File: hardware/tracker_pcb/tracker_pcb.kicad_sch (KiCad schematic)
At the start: 19 parts, among them J1 JL308-25412G01, J2 B6B-PH-K-S, J3 256-406, J5 B4B-XH-A, X1 256-402

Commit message: wip
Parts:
- JP1, JP10, JP2, JP3, JP4, JP9: now in the parts list
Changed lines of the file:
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@@
 		(unit 1)
 		(exclude_from_sim no)
-		(in_bom no)
+		(in_bom yes)
 		(on_board yes)
 		(dnp no)
@@
 		(unit 1)
 		(exclude_from_sim no)
-		(in_bom no)
+		(in_bom yes)
 		(on_board yes)
 		(dnp no)
@@
 		(unit 1)
 		(exclude_from_sim no)
-		(in_bom no)
+		(in_bom yes)
 		(on_board yes)
 		(dnp no)
@@
 		(unit 1)
 		(exclude_from_sim no)
-		(in_bom no)
+		(in_bom yes)
 		(on_board yes)
 		(dnp no)
@@
 		(unit 1)
 		(exclude_from_sim no)
-		(in_bom no)
+		(in_bom yes)
 		(on_board yes)
 		(dnp no)
@@
 		(unit 1)
 		(exclude_from_sim no)
-		(in_bom no)
-		(on_board yes)
-		(dnp no)
+		(in_bom yes)
+		(on_board yes)
+		(dnp no)

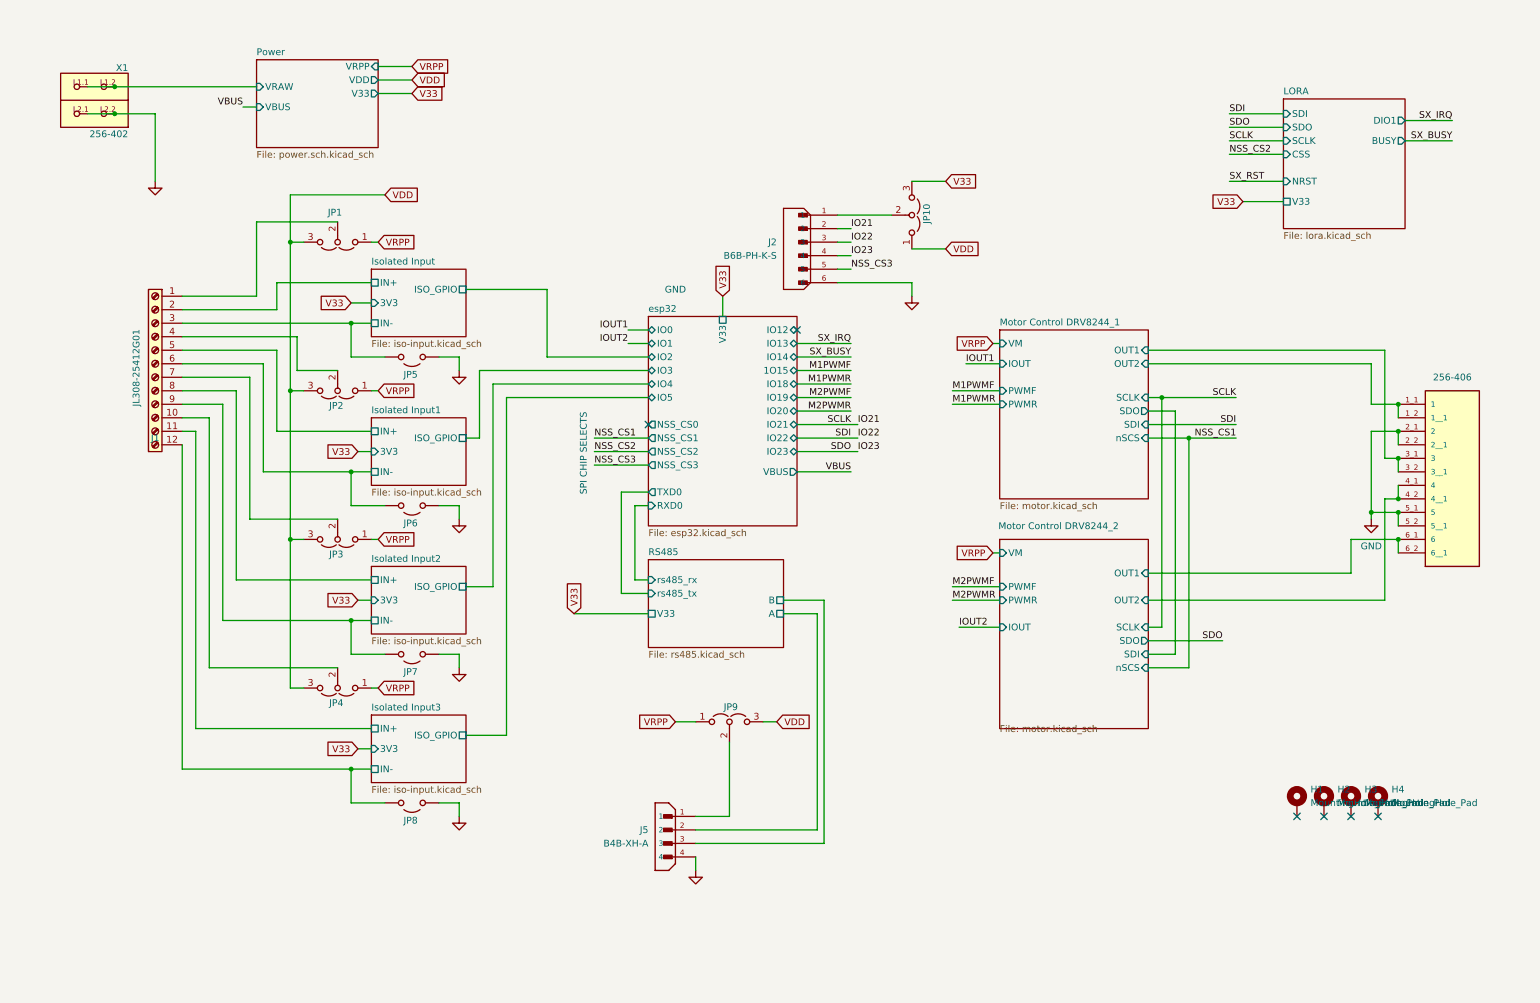
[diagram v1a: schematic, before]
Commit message: Add jst xh for inputs
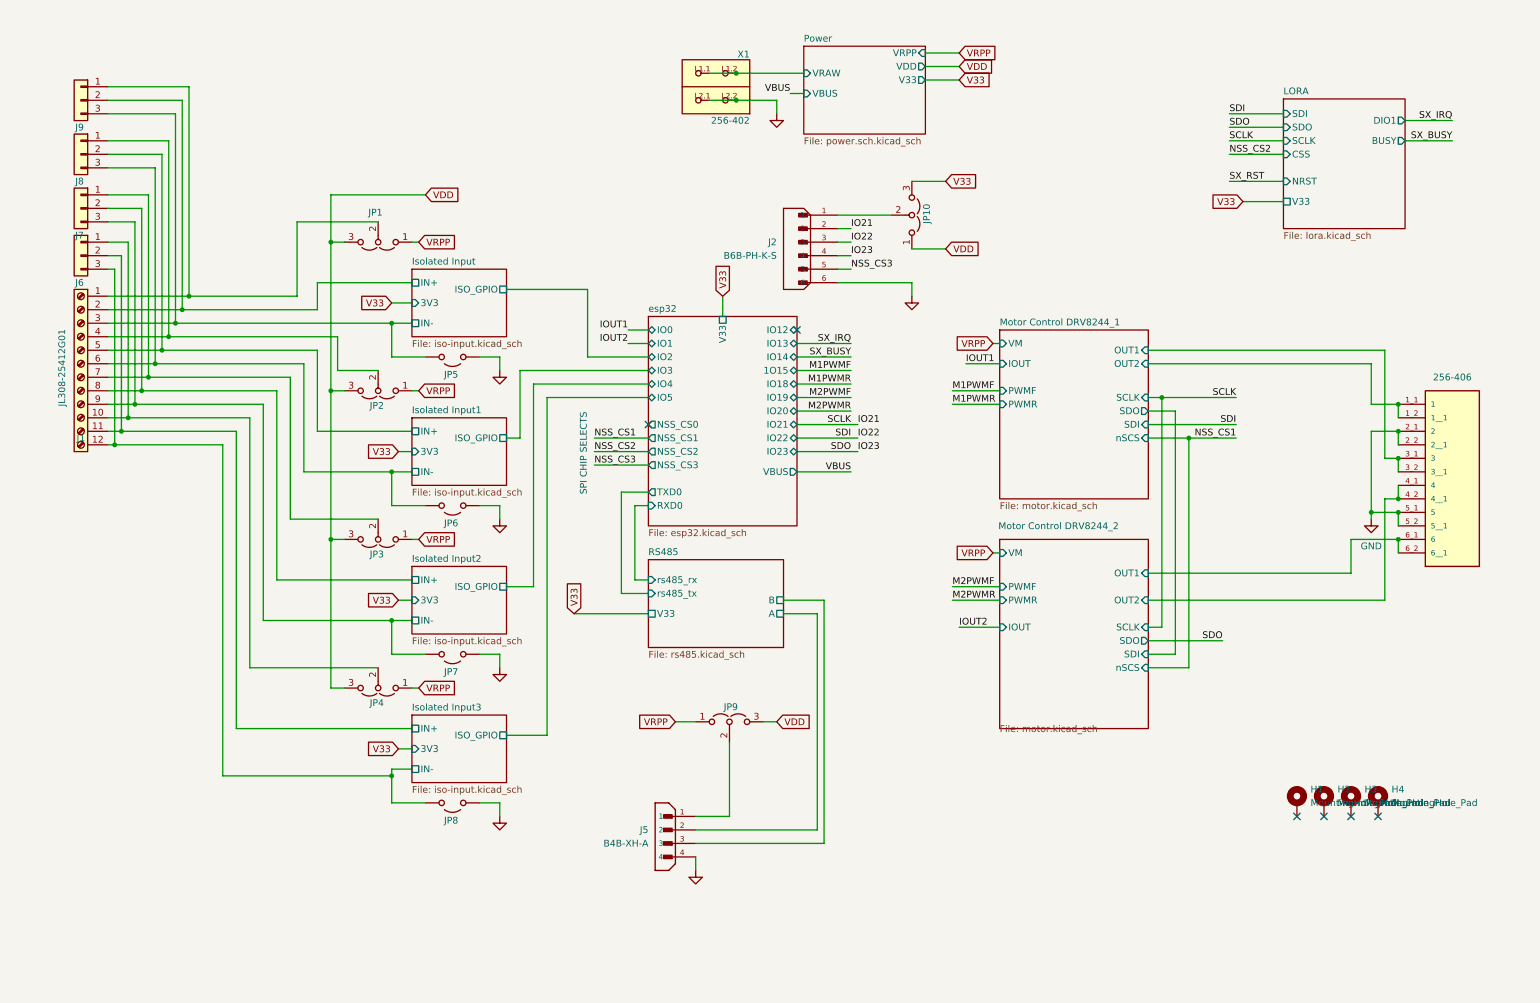
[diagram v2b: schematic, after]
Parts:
- added J6, J7, J8, J9: B3B-XH-A(LF)(SN), Connector_JST:JST_XH_B3B-XH-A_1x03_P2.50mm_Vertical, symbol symbol:B3B-XH-A
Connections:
- net Isolated Input/IN+: now also J9.2 (Pin_2)
- net Isolated Input/IN-: now also J9.3 (Pin_3)
- net Isolated Input1/IN+: now also J8.2 (Pin_2)
- net Isolated Input1/IN-: now also J8.3 (Pin_3)
- net Isolated Input2/IN+: now also J7.2 (Pin_2)
- net Isolated Input2/IN-: now also J7.3 (Pin_3)
- net Isolated Input3/IN+: now also J6.2 (Pin_2)
- net Isolated Input3/IN-: now also J6.3 (Pin_3)
- net at J1.10 (Pin_10), JP4.2 (C): now also J6.1 (Pin_1)
- net at J1.7 (Pin_7), JP3.2 (C): now also J7.1 (Pin_1)
- net at J1.1 (Pin_1), JP1.2 (C): now also J9.1 (Pin_1)
- net at J1.4 (Pin_4), JP2.2 (C): now also J8.1 (Pin_1)
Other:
- moved on the sheet: J1, JP1, JP2, JP3, JP4, JP5, JP6, JP7, JP8, X1

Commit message: Add "hardware interlock" option to use iso ins 1-4 as hardware interlock for HBRDIGE PWM signals
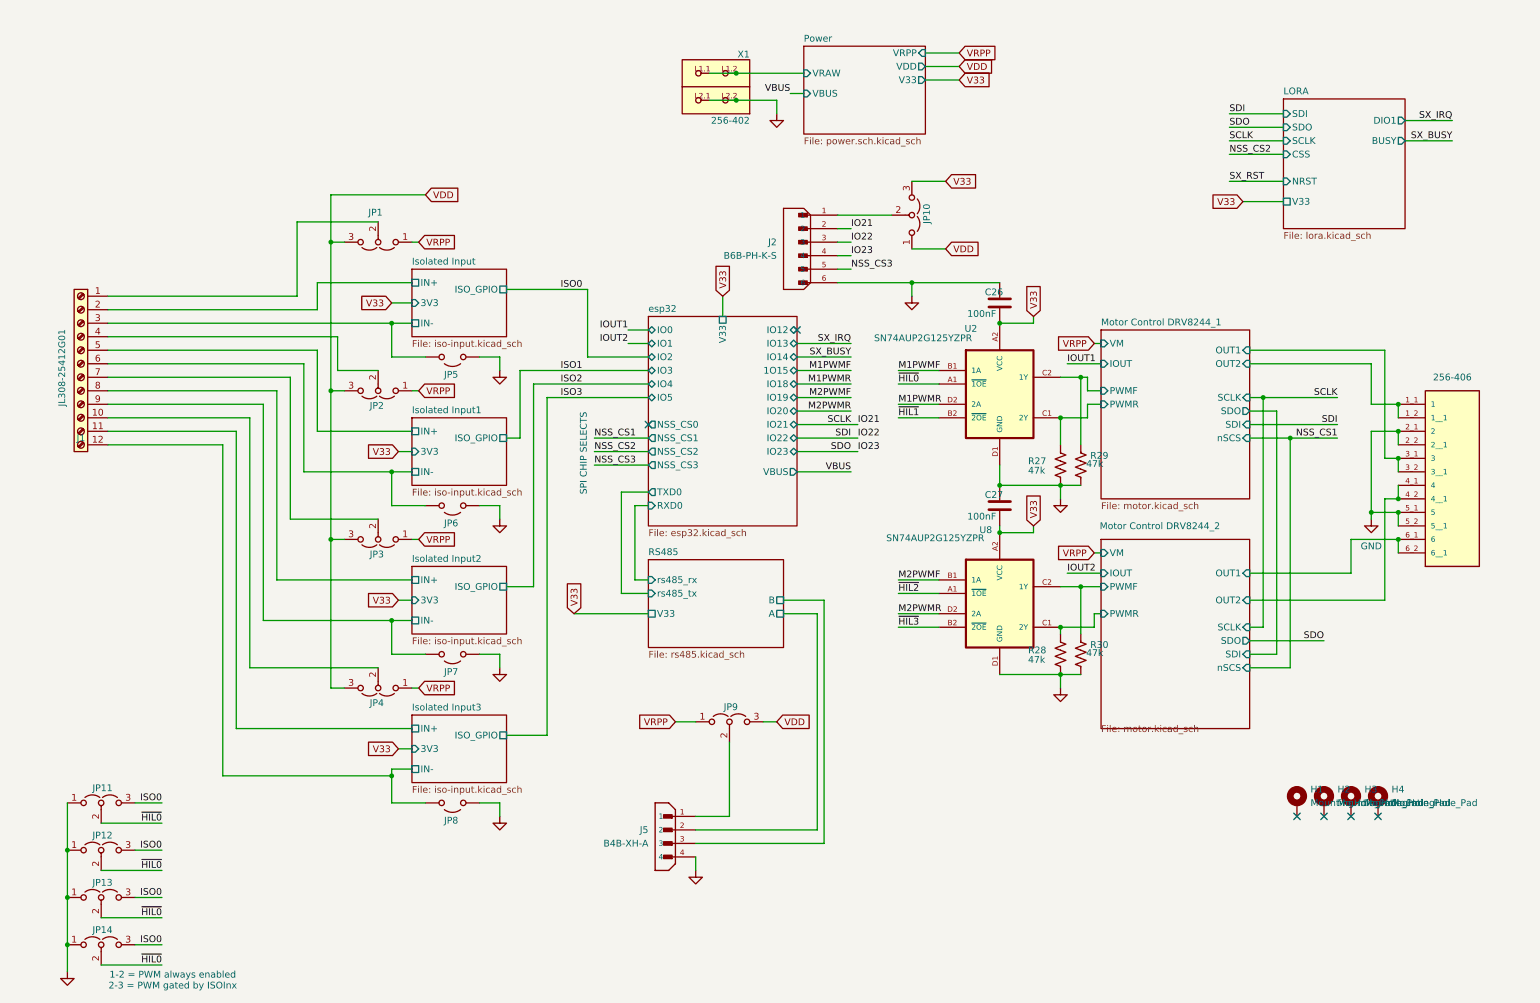
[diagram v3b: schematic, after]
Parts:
- removed J6, J7, J8, J9: B3B-XH-A(LF)(SN), Connector_JST:JST_XH_B3B-XH-A_1x03_P2.50mm_Vertical, symbol symbol:B3B-XH-A
- added C26, C27: 100nF, Capacitor_SMD:C_0603_1608Metric, symbol Device:C
- added JP11, JP12, JP13, JP14: Jumper_3_Open, Connector_PinHeader_2.00mm:PinHeader_1x03_P2.00mm_Vertical, symbol Jumper:Jumper_3_Open
- added R27, R28, R29, R30: 47k, Resistor_SMD:R_0603_1608Metric, symbol Device:R_US
- added U2, U8: SN74AUP2G125YZPR, footprint:YZP8, symbol symbol:SN74AUP2G125YZPR
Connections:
- net GND: now also C26.1, C27.1, JP11.1 (A), JP12.1 (A), JP13.1 (A), JP14.1 (A), R27.1, R28.1, R29.1, R30.1, U2.D1 (GND), U8.D1 (GND)
- net M1PWMF: now also U2.B1 (1A)
- net M1PWMR: now also U2.D2 (2A)
- net M2PWMF: now also U8.B1 (1A)
- net M2PWMR: now also U8.D2 (2A)
- net V33: now also C26.2, C27.2, U2.A2 (VCC), U8.A2 (VCC)
- new net ISO0: JP11.3 (B), JP12.3 (B), JP13.3 (B), JP14.3 (B)
- new net Motor Control DRV8244_1/PWMF: R29.2, U2.C2 (1Y)
- new net Motor Control DRV8244_1/PWMR: R27.2, U2.C1 (2Y)
- new net Motor Control DRV8244_2/PWMF: R30.2, U8.C2 (1Y)
- new net Motor Control DRV8244_2/PWMR: R28.2, U8.C1 (2Y)
- new net ~{HIL0}: JP11.2 (C), JP12.2 (C), JP13.2 (C), JP14.2 (C), U2.A1 (~{1OE})
- new net ~{HIL1}: U2.B2 (~{2OE})
- new net ~{HIL2}: U8.A1 (~{1OE})
- new net ~{HIL3}: U8.B2 (~{2OE})
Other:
- note added: "1-2 = PWM always enabled 2-3 = PWM gated by ISOInx"

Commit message: ss changes
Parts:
- removed C27: 100nF, Capacitor_SMD:C_0603_1608Metric, symbol Device:C
- added D3: LED, LED_SMD:LED_0603_1608Metric, symbol Device:LED
- added R7: 460, Resistor_SMD:R_0603_1608Metric, symbol Device:R_US
- R27, R28, R29, R30: LCSC (none) -> C25819
- U2, U8: LCSC (none) -> C2676075
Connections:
- net GND: now also C26.2; no longer C26.1
- net ISO0: no longer JP12.3 (B), JP13.3 (B), JP14.3 (B)
- net ISO1: now also JP12.3 (B)
- net ISO2: now also JP13.3 (B)
- net ISO3: now also JP14.3 (B)
- net V33: now also C26.1; no longer C26.2
- net VDD: now also R7.2
- net ~{HIL0}: no longer JP12.2 (C), JP13.2 (C), JP14.2 (C)
- net ~{HIL1}: now also JP12.2 (C)
- net ~{HIL2}: now also JP13.2 (C)
- net ~{HIL3}: now also JP14.2 (C)
- new net: D3.2 (A), R7.1
- new net NFAULT: D3.1 (K)
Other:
- sheet esp32 renamed ESP32-C6
- sheet Motor Control DRV8244_1 ports: added ~{nFAULT}, ~{nSCS}; removed IOUT, nSCS
- sheet Motor Control DRV8244_2 ports: added ~{nFAULT}, ~{nSCS}; removed IOUT, nSCS
- note added: "1-2 = PWM always enabled 2-3 = PWM gated by ~{ISOInx)"
- note added: "EXPANSION"
- note added: "H-BRIDGE INTERLOCK"
- note added: "MOTOR FAULT"
- note added: "RS485 Voltage"
- note removed: "1-2 = PWM always enabled 2-3 = PWM gated by ISOInx"
- moved on the sheet: J2, JP10, JP11, JP12, JP13, JP14

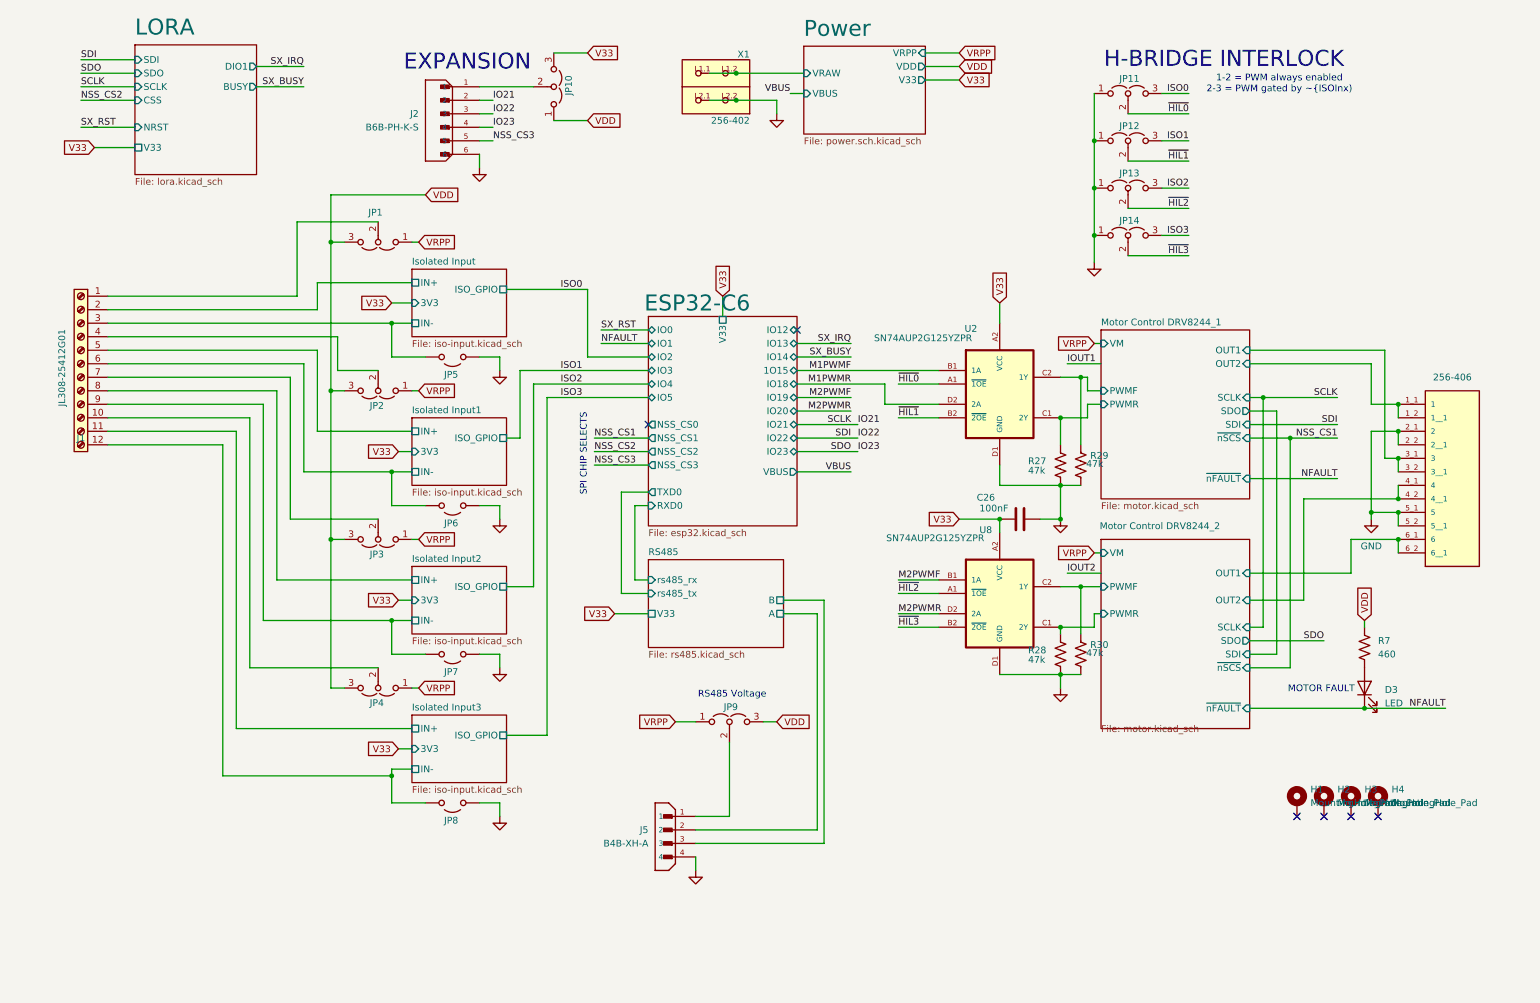
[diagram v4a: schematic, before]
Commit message: Changed to phenix screw terminal connectors
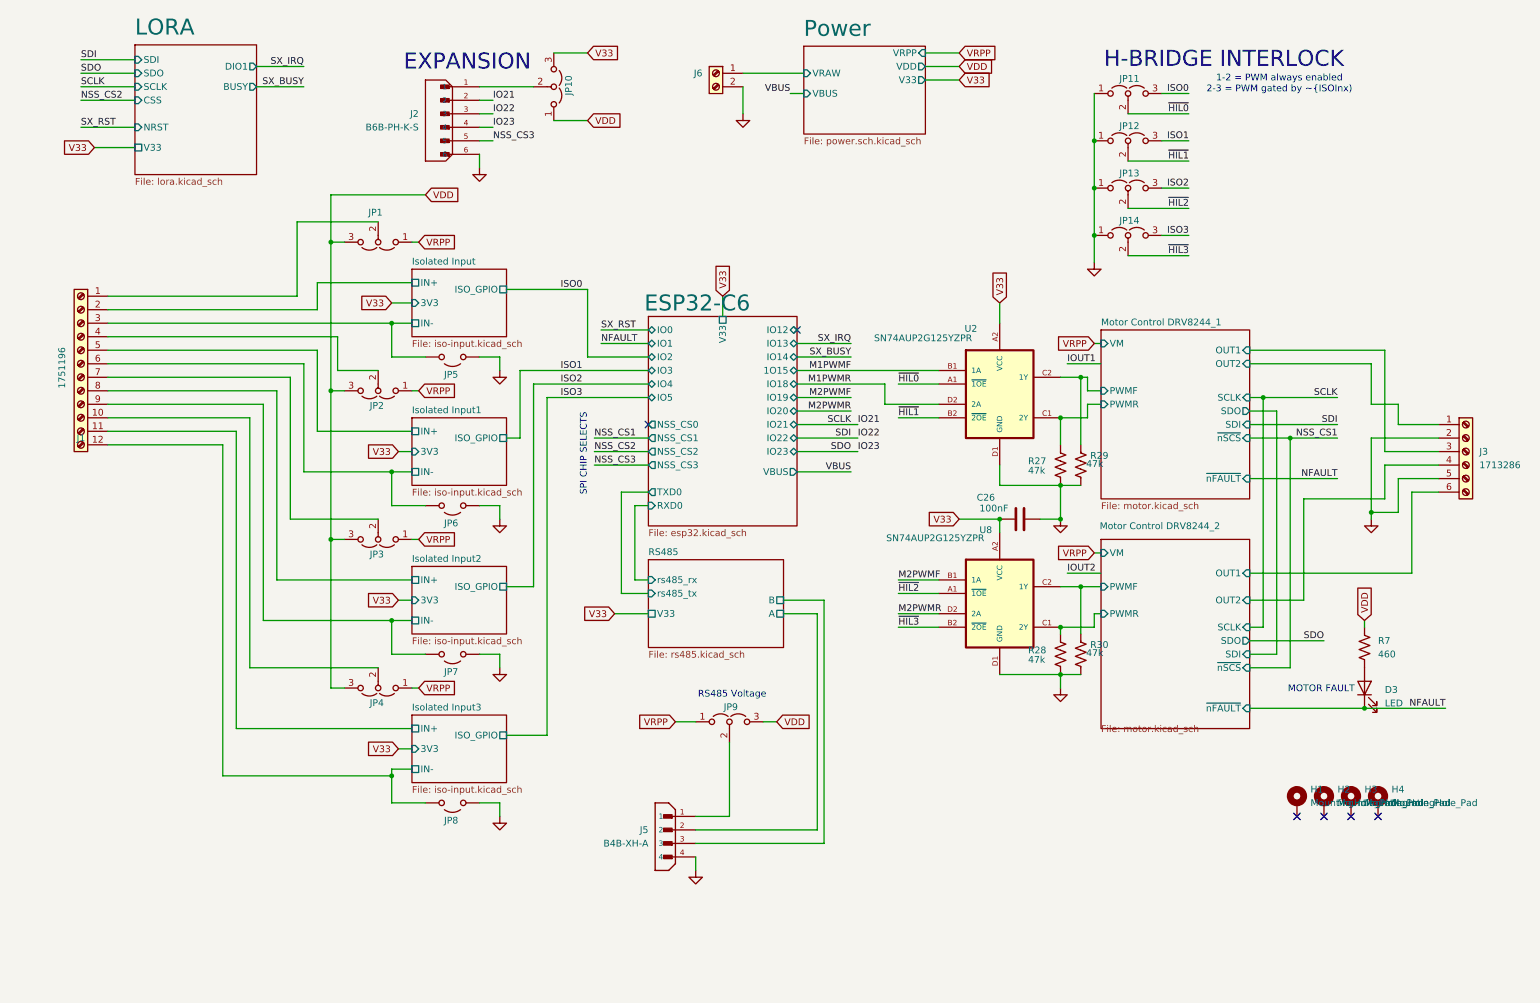
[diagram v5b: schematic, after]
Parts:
- removed J3: 256-406, footprint:WAGO_256-406, symbol symbol:256-406
- removed X1: 256-402, footprint:P-256-402, symbol symbol:256-402
- added J3: 1713286, footprint:PHOENIX_1905120, symbol Connector:Screw_Terminal_01x06
- added J6: Screw_Terminal_01x02, footprint:CONN_1720033_PXC, symbol Connector:Screw_Terminal_01x02
- J1: value JL308-25412G01 -> 1751196; footprint footprint:TE_1-282834-2 -> footprint:CONN_1751196; LCSC C2922607 -> C7164425
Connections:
- net GND: now also J3.2 (Pin_2), J3.5 (Pin_5), J6.2 (Pin_2)
- net Motor Control DRV8244_1/OUT1: now also J3.3 (Pin_3)
- net Motor Control DRV8244_1/OUT2: now also J3.1 (Pin_1)
- net Motor Control DRV8244_2/OUT1: now also J3.6 (Pin_6)
- net Motor Control DRV8244_2/OUT2: now also J3.4 (Pin_4)
- net Power/VRAW: now also J6.1 (Pin_1)
